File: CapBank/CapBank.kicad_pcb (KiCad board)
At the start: 2 copper layers, 46.5 x 66.5 mm, 23 parts, among them J1 CONN

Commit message: Changes to cap bank WIP
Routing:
- net Net-(J1-Pin_2): vias 0 -> 63
- net Net-(J1-Pin_1): vias 0 -> 63
- net Net-(C6-Pad2): vias 0 -> 36
- net Net-(C4-Pad2): vias 0 -> 36
- net Net-(C18-Pad2): vias 0 -> 36
- net Net-(C16-Pad2): vias 0 -> 36
- net Net-(C12-Pad2): vias 0 -> 36
- net Net-(C10-Pad2): vias 0 -> 36

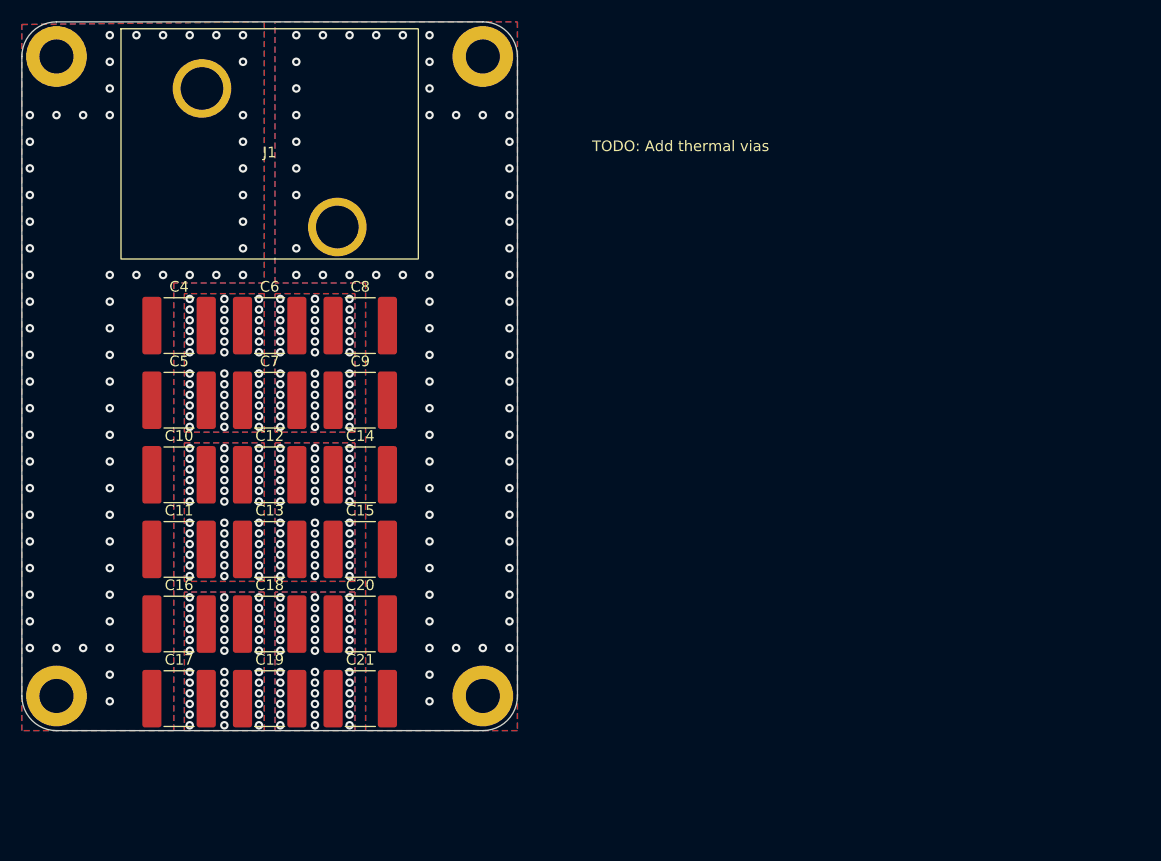
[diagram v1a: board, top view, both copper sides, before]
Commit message: Cap bank updated. Vias still WIP
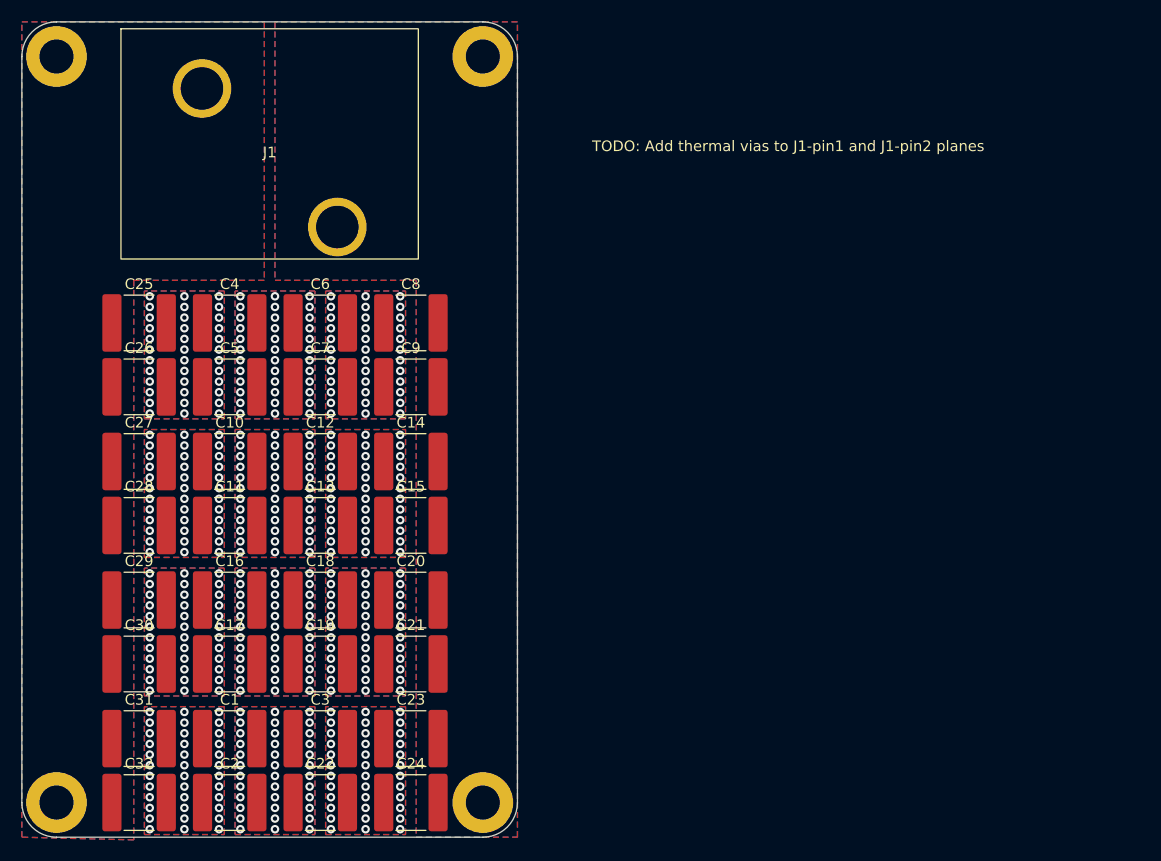
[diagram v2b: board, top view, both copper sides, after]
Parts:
- added C1: 8200p, Capacitor_SMD:C_2220_5650Metric, F.Cu at (146.2, 153.5)
- added C2: 6800p, Capacitor_SMD:C_2220_5650Metric, F.Cu at (146.2, 159.5)
- added C22: 6800p, Capacitor_SMD:C_2220_5650Metric, F.Cu at (154.8, 159.5)
- added C23: 8200p, Capacitor_SMD:C_2220_5650Metric, F.Cu at (163.2, 153.5)
- added C24: 6800p, Capacitor_SMD:C_2220_5650Metric, F.Cu at (163.2, 159.5)
- added C25: 8200p, Capacitor_SMD:C_2220_5650Metric, F.Cu at (137.8, 114.5)
- added C26: 6800p, Capacitor_SMD:C_2220_5650Metric, F.Cu at (137.8, 120.5)
- added C27: 8200p, Capacitor_SMD:C_2220_5650Metric, F.Cu at (137.8, 127.5)
- added C28: 6800p, Capacitor_SMD:C_2220_5650Metric, F.Cu at (137.8, 133.5)
- added C29: 8200p, Capacitor_SMD:C_2220_5650Metric, F.Cu at (137.8, 140.5)
- added C3: 8200p, Capacitor_SMD:C_2220_5650Metric, F.Cu at (154.8, 153.5)
- added C30: 6800p, Capacitor_SMD:C_2220_5650Metric, F.Cu at (137.8, 146.5)
- added C31: 8200p, Capacitor_SMD:C_2220_5650Metric, F.Cu at (137.8, 153.5)
- added C32: 6800p, Capacitor_SMD:C_2220_5650Metric, F.Cu at (137.8, 159.5)
- moved H3 10.0 mm to (130.0, 159.5)
- moved H4 10.0 mm to (170.0, 159.5)
- moved C17 5.76 mm to (146.2, 146.5)
- moved C19 5.76 mm to (154.8, 146.5)
- moved C21 5.76 mm to (163.2, 146.5)
- moved C11 5.26 mm to (146.2, 133.5)
- moved C13 5.26 mm to (154.8, 133.5)
- moved C15 5.26 mm to (163.2, 133.5)
- moved C16 5.26 mm to (146.2, 140.5)
- moved C18 5.26 mm to (154.8, 140.5)
- moved C20 5.26 mm to (163.2, 140.5)
- moved C10 4.91 mm to (146.2, 127.5)
- moved C12 4.91 mm to (154.8, 127.5)
- moved C14 4.91 mm to (163.2, 127.5)
- moved C5 4.91 mm to (146.2, 120.5)
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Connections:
- C10 pad 1: Net-(J1-Pin_1) -> Net-(C10-Pad1)
- C11 pad 1: Net-(J1-Pin_1) -> Net-(C10-Pad1)
- C16 pad 1: Net-(J1-Pin_1) -> Net-(C16-Pad1)
- C17 pad 1: Net-(J1-Pin_1) -> Net-(C16-Pad1)
- C4 pad 1: Net-(J1-Pin_1) -> Net-(C25-Pad2)
- C5 pad 1: Net-(J1-Pin_1) -> Net-(C25-Pad2)
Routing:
- net Net-(J1-Pin_2): vias 63 -> 0
- net Net-(J1-Pin_1): vias 63 -> 0
- net Net-(C25-Pad2): vias 0 -> 36
- net Net-(C22-Pad2): vias 0 -> 36
- net Net-(C16-Pad1): vias 0 -> 36
- net Net-(C10-Pad1): vias 0 -> 36
- net Net-(C1-Pad2): vias 0 -> 36
- net Net-(C1-Pad1): vias 0 -> 36
- added copper zone on B.Cu, net Net-(C1-Pad1)
- added copper zone on F.Cu, net Net-(C1-Pad1)
- added copper zone on B.Cu, net Net-(C1-Pad2)
- added copper zone on F.Cu, net Net-(C1-Pad2)
- added copper zone on B.Cu, net Net-(C10-Pad1)
- added copper zone on F.Cu, net Net-(C10-Pad1)
- added copper zone on B.Cu, net Net-(C16-Pad1)
- added copper zone on F.Cu, net Net-(C16-Pad1)
- added copper zone on B.Cu, net Net-(C22-Pad2)
- added copper zone on F.Cu, net Net-(C22-Pad2)
- added copper zone on B.Cu, net Net-(C25-Pad2)
- added copper zone on F.Cu, net Net-(C25-Pad2)
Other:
- board size 46.5 x 66.5 mm -> 46.5 x 76.5 mm
- board text added: "TODO: Add thermal vias to J1-pin1 and J1-pin2 planes"
- board text removed: "TODO: Add thermal vias"

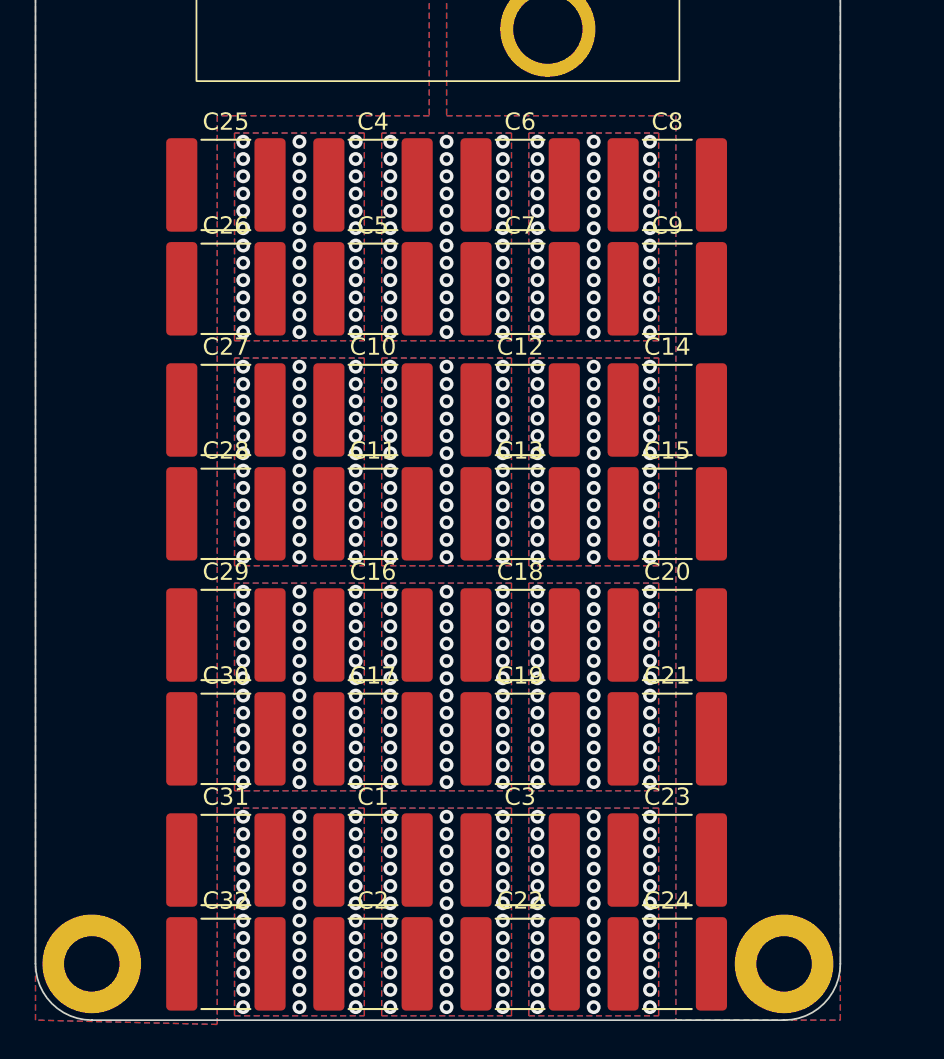
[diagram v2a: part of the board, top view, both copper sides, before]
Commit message: Added transformer pcb
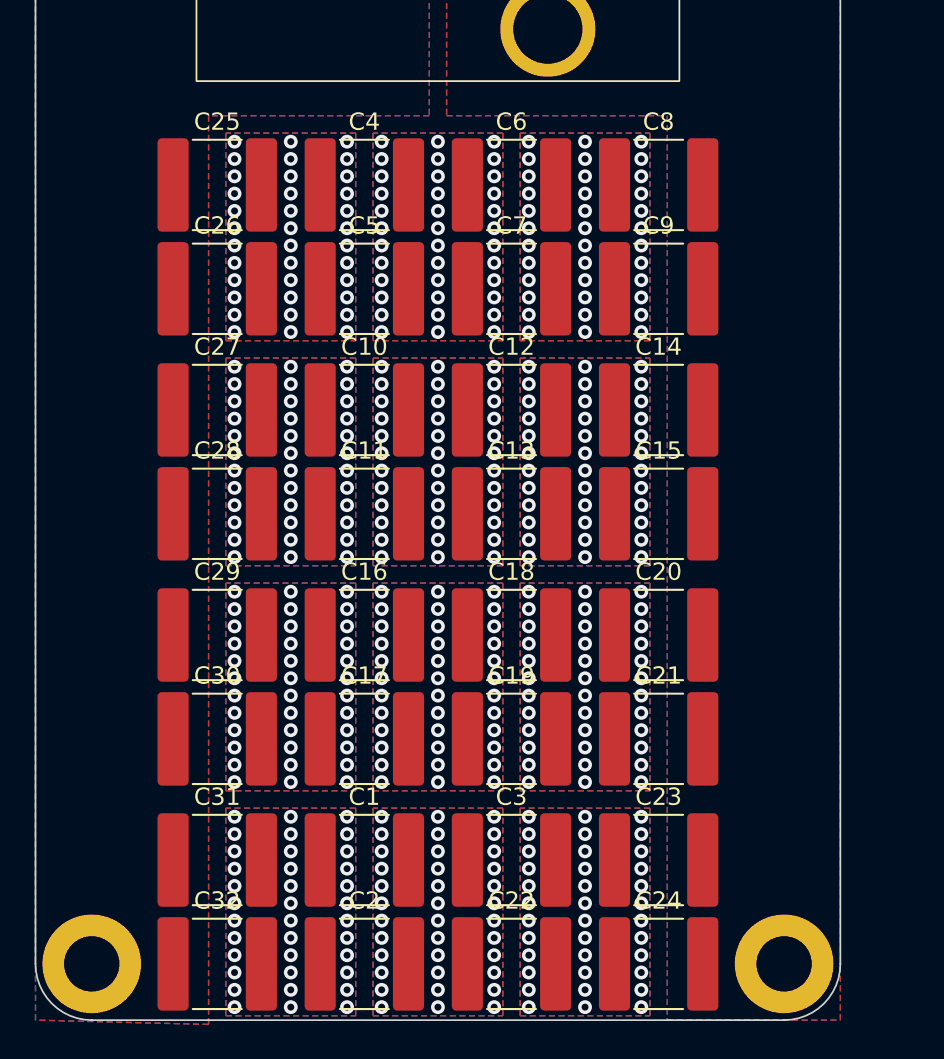
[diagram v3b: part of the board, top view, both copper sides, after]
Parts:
- moved C1 0.50 mm to (145.8, 153.5)
- moved C10 0.50 mm to (145.8, 127.5)
- moved C11 0.50 mm to (145.8, 133.5)
- moved C12 0.50 mm to (154.2, 127.5)
- moved C13 0.50 mm to (154.2, 133.5)
- moved C14 0.50 mm to (162.8, 127.5)
- moved C15 0.50 mm to (162.8, 133.5)
- moved C16 0.50 mm to (145.8, 140.5)
- moved C17 0.50 mm to (145.8, 146.5)
- moved C18 0.50 mm to (154.2, 140.5)
- moved C19 0.50 mm to (154.2, 146.5)
- moved C2 0.50 mm to (145.8, 159.5)
- moved C20 0.50 mm to (162.8, 140.5)
- moved C21 0.50 mm to (162.8, 146.5)
- moved C22 0.50 mm to (154.2, 159.5)
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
